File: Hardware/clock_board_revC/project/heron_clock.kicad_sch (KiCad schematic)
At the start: 110 parts, among them J1 5V_IN, J10 PPS_B200_2, J2 PPS_IN, J3 REF_B210_1, J4 REF_B210_2, J5 REF_B200_1, J6 REF_B200_2, J7 PPS_B210_1, J8 PPS_B210_2, J9 PPS_B200_1, U1 LP5907MFX-3.3/NOPB, U2 TLV75533PDBVR, U3 SiT5155AI-FK-33E0-10.000000, U4 LMK1C1104PWR, U5 SN74LVC1G17DBVR, U6 SN74LVC125APWR

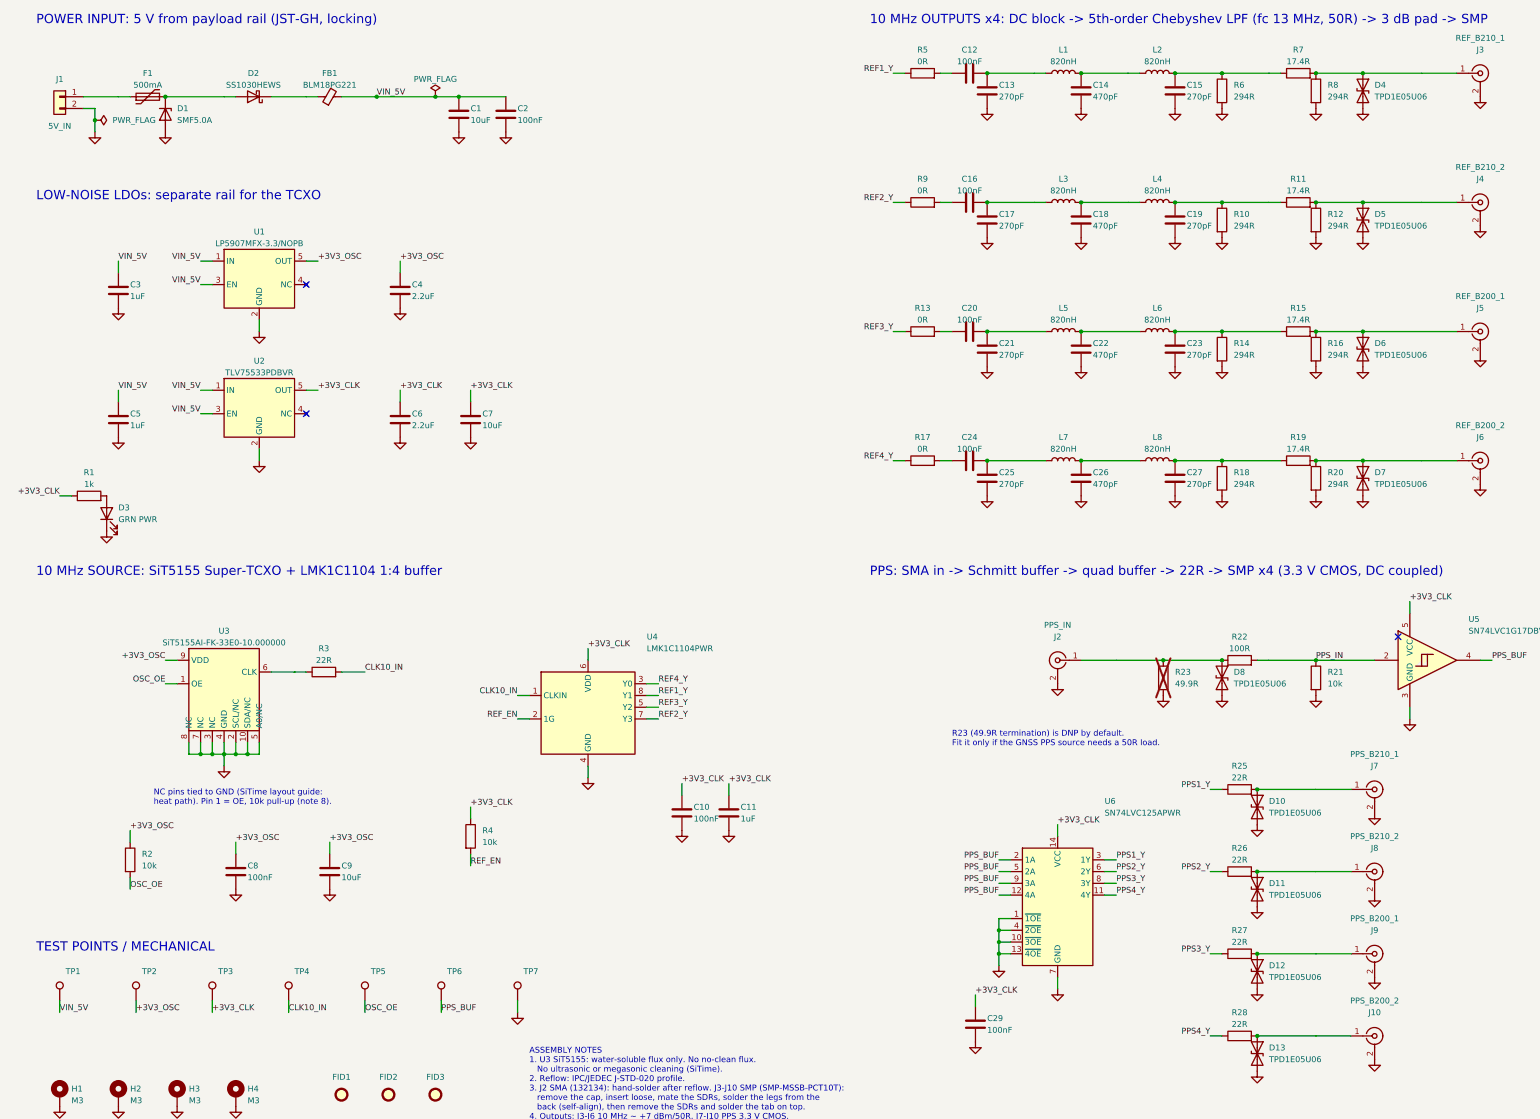
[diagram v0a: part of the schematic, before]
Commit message: update pcb silk screen and rack cad
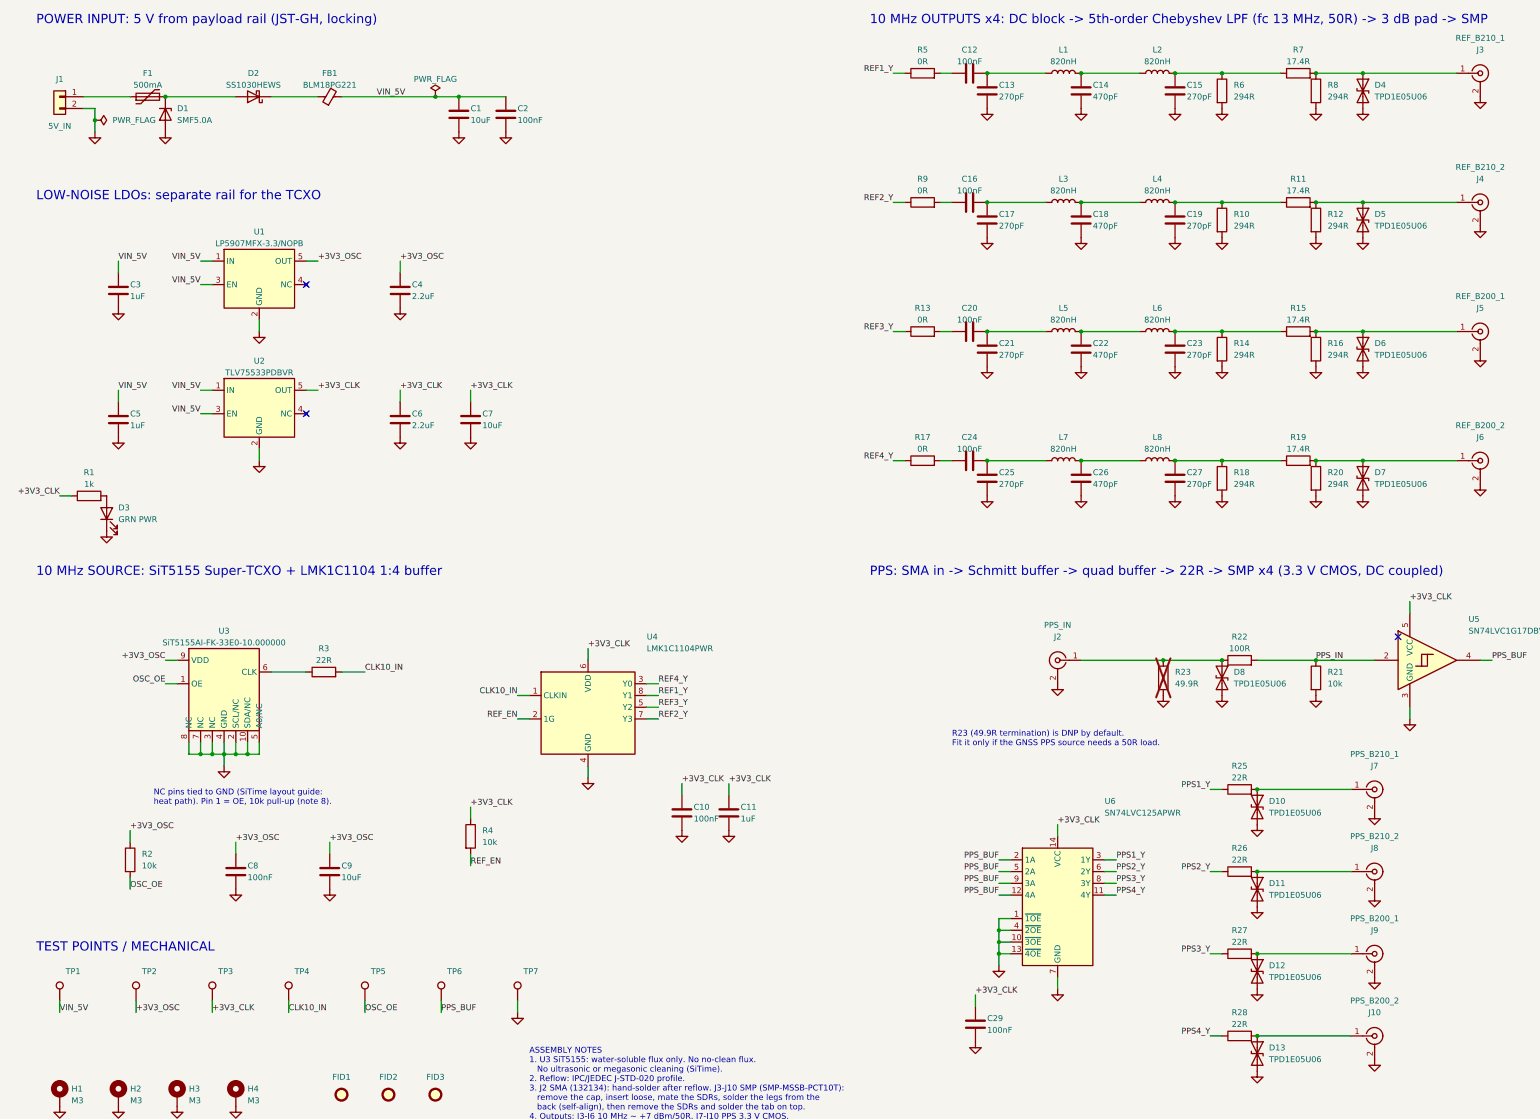
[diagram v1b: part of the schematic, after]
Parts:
- R2, R21, R4: MPN RC0603FR-0710KL -> AC0603FR-0710KL
- R22: MPN RC0603FR-07100RL -> AC0603FR-07100RL
